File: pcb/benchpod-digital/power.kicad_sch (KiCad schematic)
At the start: 72 parts, among them J4 DB2ERC-3.81-2P-BK, J5 DB2ERC-3.81-2P-BK, J6 DB2ERC-3.81-2P-BK, U26 TPS259470ARPWR, U27 TPS259470ARPWR, U29 INA226AIDGSR, U30 TPS82130SILR, U31 AP2112K-1.2, U32 AP2112K-2.5TRG1, U33 INA226AIDGSR, U52 AP2112K-1.8TRG1, U56 TCA9554PWR

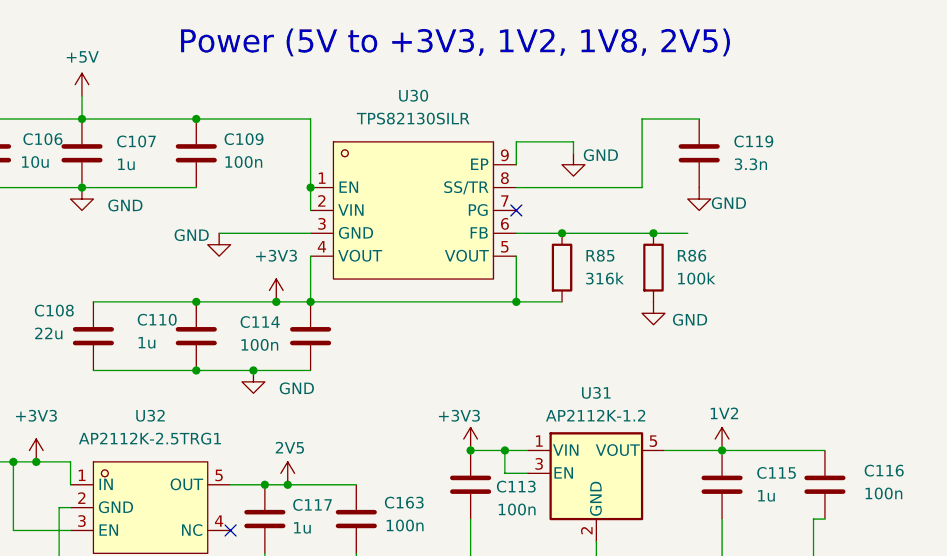
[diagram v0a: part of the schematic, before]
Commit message: digital v3r3: 3.3 V buck U30 becomes TPS62130A plus a 2.2 uH inductor
The TPS82130 module is a TPS62130 with a 1 uH inductor inside. Discrete, per
the TPS62130 datasheet typical application (figure 9-1, table 9-1):

- U30 TPS62130ARGTR (C337502, $0.80, KiCad VQFN-16 footprint with thermal
  vias); L1 2.2 uH 4x4 shielded FNR4030S2R2MT (C167869, 3.2 A, 5.8 A sat,
  39 mohm). 2.2 uH + 22 uF is the datasheet's standard LC combination.
- PVIN/AVIN and EN on +5V; VOS on +3V3; FB divider R85 316k / R86 100k
  unchanged (FB is 0.8 V on both, 3.33 V out); SS/TR C119 3.3 nF unchanged;
  DEF and FSW on GND (nominal output, 2.5 MHz); PG unconnected, so the A
  version's PG behavior does not matter.
- Existing caps stay: C107/C109 on +5V, C106 10u input, C108 22u output.

Saves about $3.90 per board at qty 1 ($4.76 module vs $0.85). BOM: one new
line (the inductor). Layout: keep the PVIN cap, IC and L1 loop tight, AGND and
PGND straight to the pad and ground plane, VOS and FB away from SW, no traces
under L1 (datasheet section 11).

Co-Authored-By: Claude Opus 5.5 <noreply@anthropic.com>
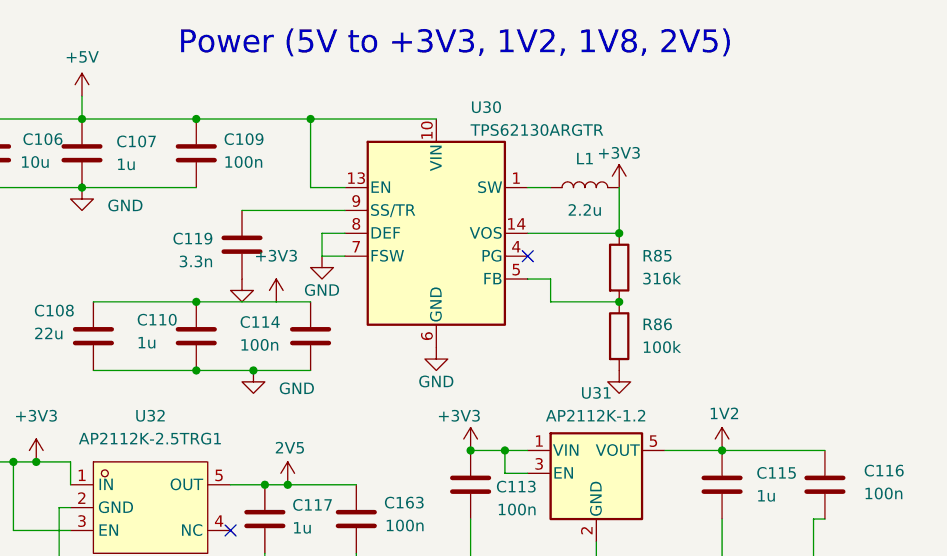
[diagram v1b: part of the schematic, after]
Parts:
- removed U30: TPS82130SILR, lcsc:USIP-8_L3.0-W2.8-P0.65-TL-EP, symbol lcsc_lib:TPS82130SILR
- added L1: 2.2u, lcsc_footprints:C167869_IND-SMD_L4.0-W4.0_FNR40XXS, symbol Device:L
- added U30: TPS62130ARGTR, Package_DFN_QFN:VQFN-16-1EP_3x3mm_P0.5mm_EP1.68x1.68mm_ThermalVias, symbol Regulator_Switching:TPS62130A
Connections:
- net +3V3: now also R85.1, L1.2, U30.14 (VOS); no longer R85.2
- net +5V: now also U30.10 (VIN), U30.11 (VIN), U30.12 (VIN), U30.13 (EN)
- net GND: now also U30.15 (GND), U30.16 (GND), U30.17 (GND), U30.6 (GND), U30.7 (FSW), U30.8 (DEF)
- net at R86.1: now also R85.2, U30.5 (FB); no longer R85.1
- net at C119.1: now also U30.9 (SS/TR)
- new net: L1.1, U30.1 (SW), U30.2 (SW), U30.3 (SW)
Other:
- moved on the sheet: C119, R85, R86
